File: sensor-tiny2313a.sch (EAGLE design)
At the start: 36 parts, among them IC1 TINY2313-*P*, M1 NRF24L01P-M, M2 DHT22, Q2 IRLML2502, U1 MCP1640C

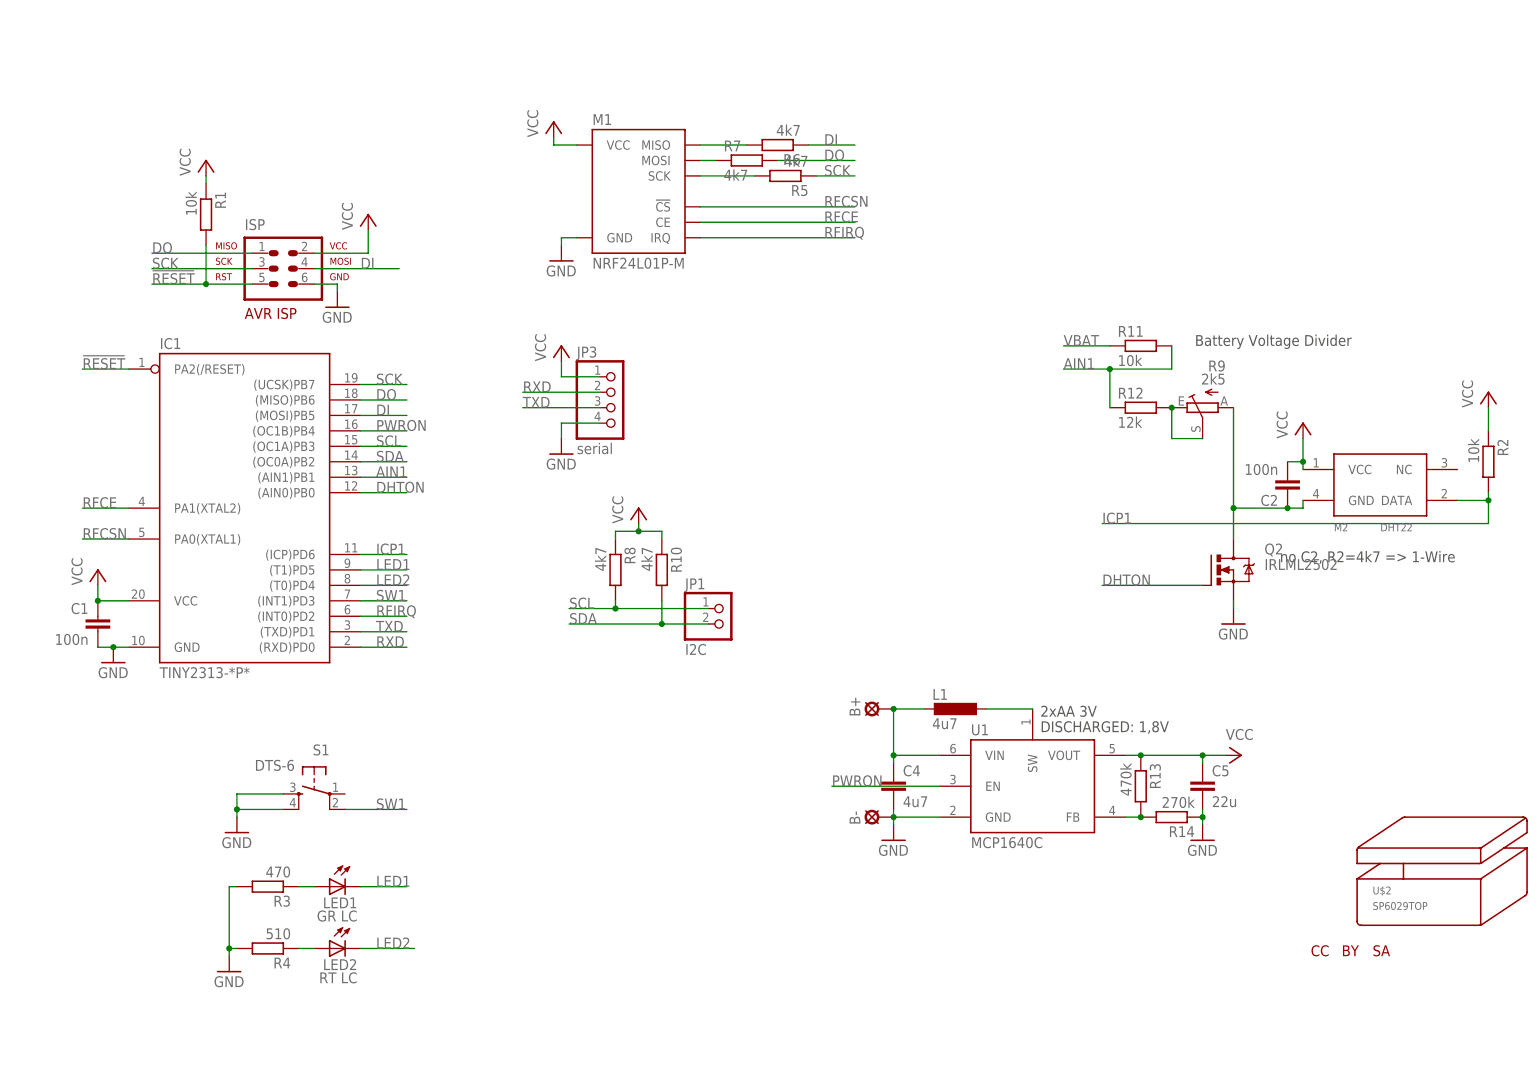
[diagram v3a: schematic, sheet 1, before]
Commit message: attiny so20 package
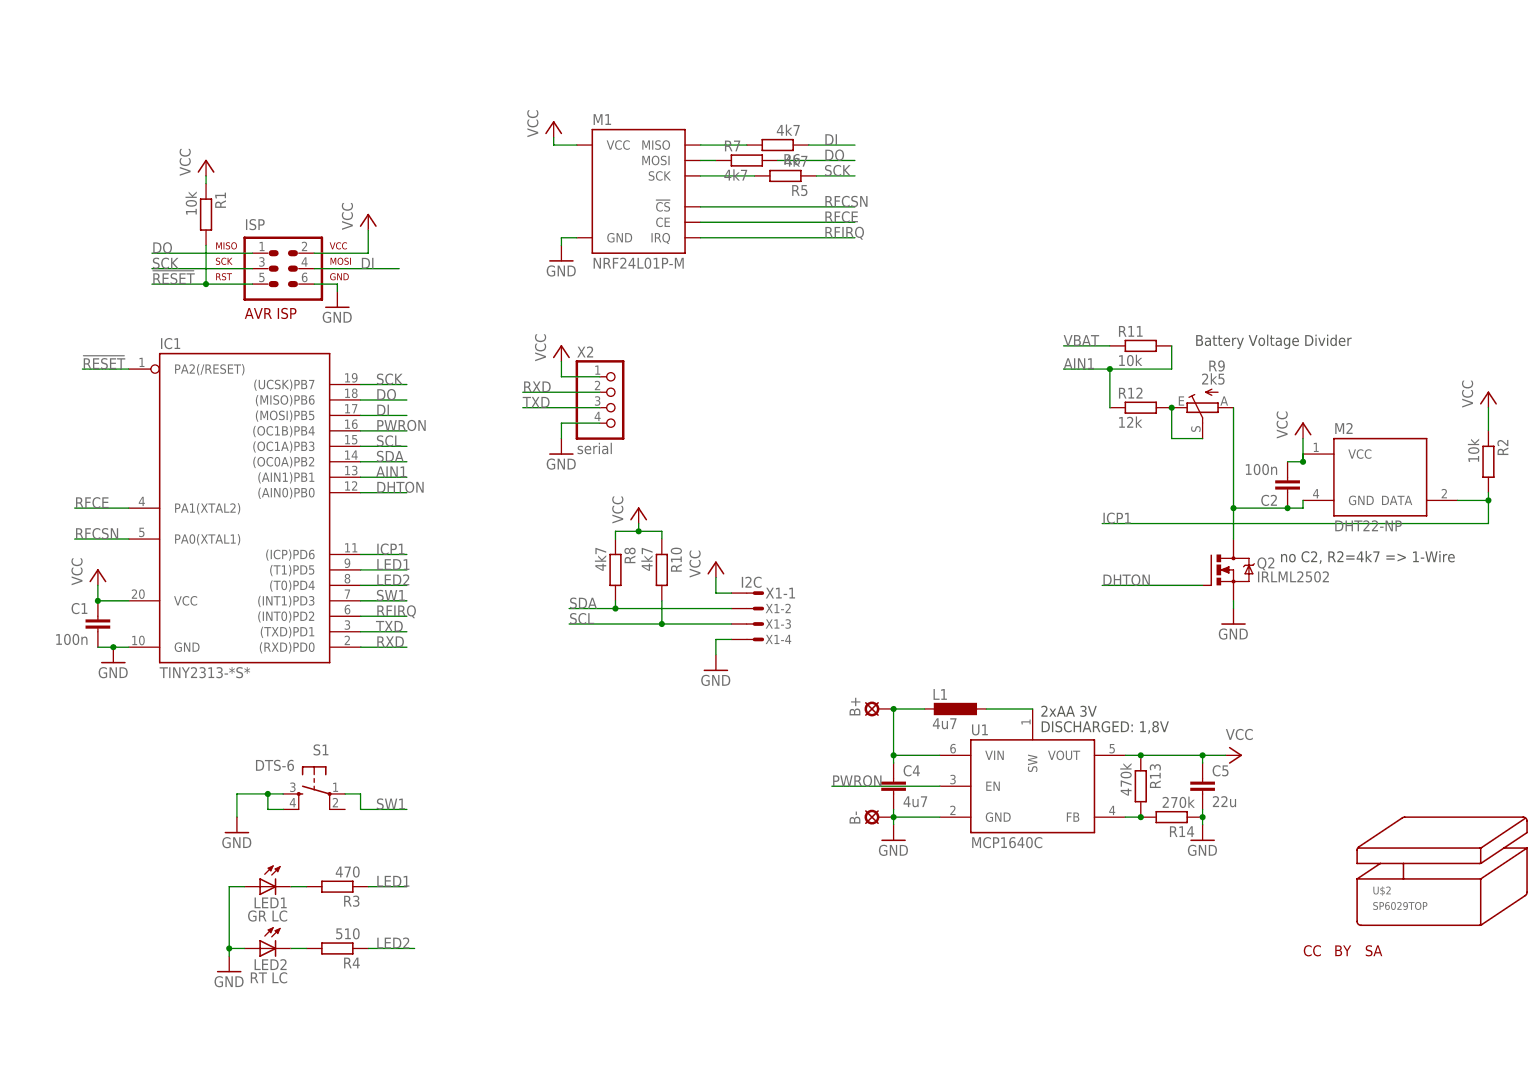
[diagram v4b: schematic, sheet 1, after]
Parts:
- removed JP1: I2C, pinhead-mod:PINHD-1X2_2.54
- added X1: I2C, con-amp-micromatch:MICROMATCH-4
- IC1: value TINY2313-*P* -> TINY2313-*S*; device avr-7:TINY2313-*P* -> avr-7:TINY2313-*S*
- M2: value DHT22 -> DHT22-NP; device modules:DHT22 -> modules:DHT22-NP
- R9: device pot:TRIM_EU-CA6V -> pot:TRIM_EU-CA6H
- U$1: value CC-TOP-HALF -> CC-TPLACE-HALF; device creative-commons:CC-TOP-HALF -> creative-commons:CC-TPLACE-HALF
- U$3: value BY-TOP-HALF -> BY-TPLACE-HS; device creative-commons:BY-TOP-HALF -> creative-commons:BY-TPLACE-HS
- U$4: value SA-TOP-HALF -> SA-TPLACE-HALF; device creative-commons:SA-TOP-HALF -> creative-commons:SA-TPLACE-HALF
- renumbered JP3 to X2
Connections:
- removed net N$13: LED1.A, R3.1
- new net N$3: LED1.C, R3.2
- net GND: now also LED1.A, LED2.A, X1-4.S; no longer R3.2, R4.2
- net LED1: now also R3.1; no longer LED1.C
- net LED2: now also R4.1; no longer LED2.C
- net N$1: now also LED2.C, R4.2; no longer LED2.A, R4.1
- net SCL: now also R10.2, X1-3.S; no longer JP1.1, R8.2
- net SDA: now also R8.2, X1-2.S; no longer JP1.2, R10.2
- net SW1: now also S1.1; no longer S1.2
- net VCC: now also X1-1.S
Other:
- moved on the sheet: LED1, LED2, R3, R4

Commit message: deleted second sch sheet with case scribbling
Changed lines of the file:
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@@
 <part name="R6" library="rcl" deviceset="R-EU_" device="R0603" value="4k7"/>
 <part name="R7" library="rcl" deviceset="R-EU_" device="R0603" value="4k7"/>
-<part name="FRAME1" library="frames" deviceset="A4L-LOC" device=""/>
 <part name="IC1" library="avr-7" deviceset="TINY2313*" device="-*S*" value="TINY2313-*S*"/>
 <part name="U$2" library="strapubox" deviceset="SP6029" device="TOP"/>
@@
 </nets>
 </sheet>
-<sheet>
-<plain>
-<wire x1="162.6" y1="55.6" x2="206.4" y2="55.6" width="0.4064" layer="97"/>
-<wire x1="206.4" y1="55.6" x2="206.4" y2="131.4" width="0.4064" layer="97"/>
-<wire x1="206.4" y1="131.4" x2="162.6" y2="131.4" width="0.4064" layer="97"/>
-<wire x1="162.6" y1="131.4" x2="162.6" y2="55.6" width="0.4064" layer="97"/>
-<circle x="172" y="64.5" radius="4" width="0.4064" layer="97"/>
-<circle x="197" y="64.5" radius="4" width="0.4064" layer="97"/>
-<circle x="172" y="122.5" radius="4" width="0.4064" layer="97"/>
-<circle x="197" y="122.5" radius="4" width="0.4064" layer="97"/>
-<rectangle x1="55" y1="38" x2="105" y2="52" layer="97" rot="R270"/>
-<rectangle x1="69" y1="38" x2="119" y2="52" layer="97" rot="R90"/>
-<rectangle x1="26" y1="8" x2="41" y2="33" layer="97" rot="R180"/>
-<rectangle x1="39.5" y1="57" x2="53.5" y2="90" layer="97" rot="R180"/>
-<wire x1="12.1" y1="7.1" x2="55.9" y2="7.1" width="0.4064" layer="97"/>
-<wire x1="55.9" y1="7.1" x2="55.9" y2="100.9" width="0.4064" layer="97"/>
-<wire x1="55.9" y1="100.9" x2="12.1" y2="100.9" width="0.4064" layer="97"/>
-<wire x1="12.1" y1="100.9" x2="12.1" y2="7.1" width="0.4064" layer="97"/>
-<circle x="50.5" y="12.5" radius="4.5" width="0.4064" layer="97"/>
-<circle x="17.5" y="95.5" radius="4.5" width="0.4064" layer="97"/>
-<circle x="17.5" y="12.5" radius="4.5" width="0.4064" layer="97"/>
-<circle x="50.5" y="95.5" radius="4.5" width="0.4064" layer="97"/>
-<circle x="20" y="21" radius="4" width="0.4064" layer="97"/>
-<circle x="48" y="21" radius="4" width="0.4064" layer="97"/>
-<circle x="20" y="87" radius="4" width="0.4064" layer="97"/>
-<circle x="48" y="87" radius="4" width="0.4064" layer="97"/>
-<rectangle x1="13" y1="33" x2="37.5" y2="87" layer="97"/>
-</plain>
-<instances>
-<instance part="FRAME1" gate="G$1" x="0" y="0"/>
-</instances>
-<busses>
-</busses>
-<nets>
-</nets>
-</sheet>
 </sheets>
-<errors>
-</errors>
 </schematic>
 </drawing>

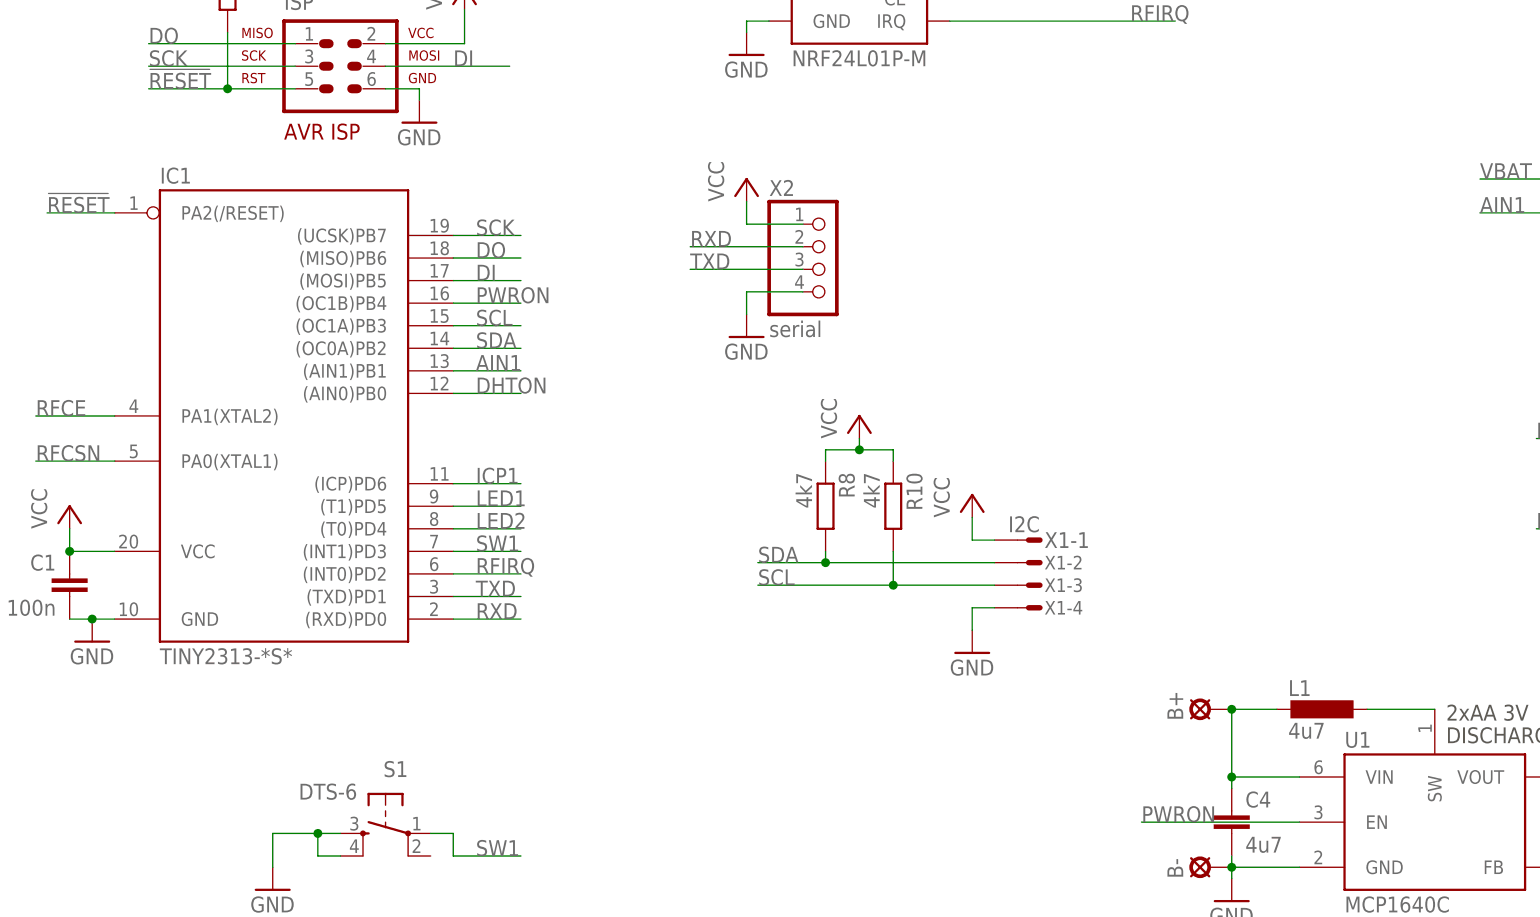
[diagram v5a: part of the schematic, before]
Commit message: renamed ic1->u1, u1->u2
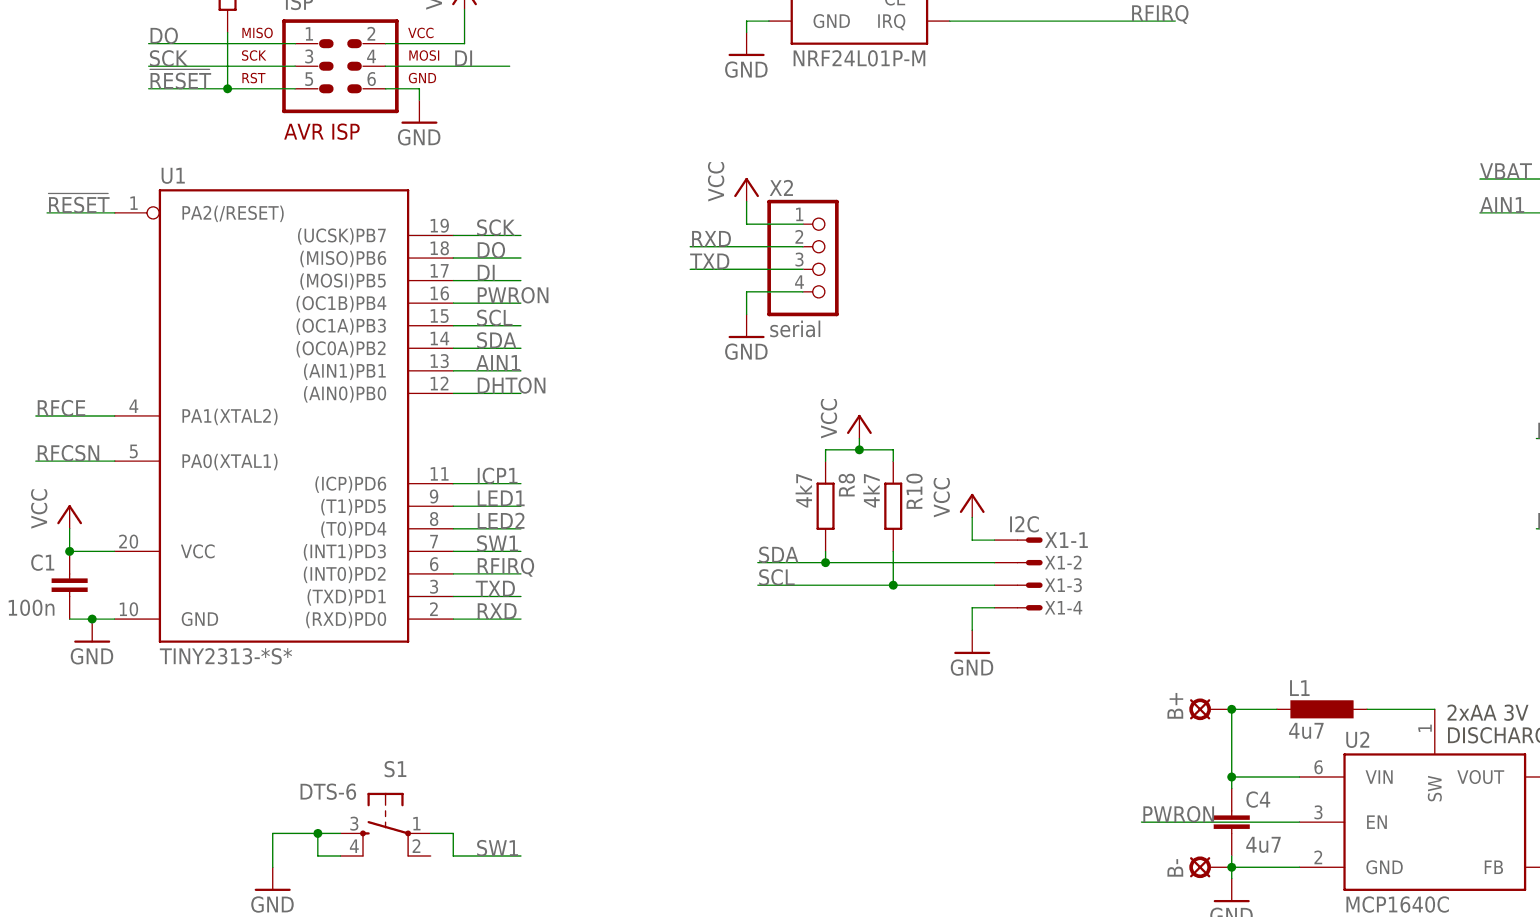
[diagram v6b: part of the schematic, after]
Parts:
- removed IC1: TINY2313-*S*, avr-7:TINY2313-*S*
- added U2: MCP1640C, karlnet-parts:MCP1640
- U1: value MCP1640C -> TINY2313-*S*; device karlnet-parts:MCP1640 -> avr-7:TINY2313-*S*
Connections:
- net !RESET: now also U1.PA2(/RESET); no longer IC1.PA2(/RESET)
- net AIN1: now also U1.(AIN1)PB1; no longer IC1.(AIN1)PB1
- net DHTON: now also U1.(AIN0)PB0; no longer IC1.(AIN0)PB0
- net DI: now also U1.(MOSI)PB5; no longer IC1.(MOSI)PB5
- net DO: now also U1.(MISO)PB6; no longer IC1.(MISO)PB6
- net GND: now also U2.GND; no longer IC1.GND
- net ICP1: now also U1.(ICP)PD6; no longer IC1.(ICP)PD6
- net LED1: now also U1.(T1)PD5; no longer IC1.(T1)PD5
- net LED2: now also U1.(T0)PD4; no longer IC1.(T0)PD4
- net N$8: now also U2.SW; no longer U1.SW
- net N$9: now also U2.FB; no longer U1.FB
- net PWRON: now also U1.(OC1B)PB4, U2.EN; no longer IC1.(OC1B)PB4, U1.EN
- net RFCE: now also U1.PA1(XTAL2); no longer IC1.PA1(XTAL2)
- net RFCSN: now also U1.PA0(XTAL1); no longer IC1.PA0(XTAL1)
- net RFIRQ: now also U1.(INT0)PD2; no longer IC1.(INT0)PD2
- net RXD: now also U1.(RXD)PD0; no longer IC1.(RXD)PD0
- net SCK: now also U1.(UCSK)PB7; no longer IC1.(UCSK)PB7
- net SCL: now also U1.(OC1A)PB3; no longer IC1.(OC1A)PB3
- net SDA: now also U1.(OC0A)PB2; no longer IC1.(OC0A)PB2
- net SW1: now also U1.(INT1)PD3; no longer IC1.(INT1)PD3
- net TXD: now also U1.(TXD)PD1; no longer IC1.(TXD)PD1
- net VBAT: now also U2.VIN; no longer U1.VIN
- net VCC: now also U1.VCC, U2.VOUT; no longer IC1.VCC, U1.VOUT

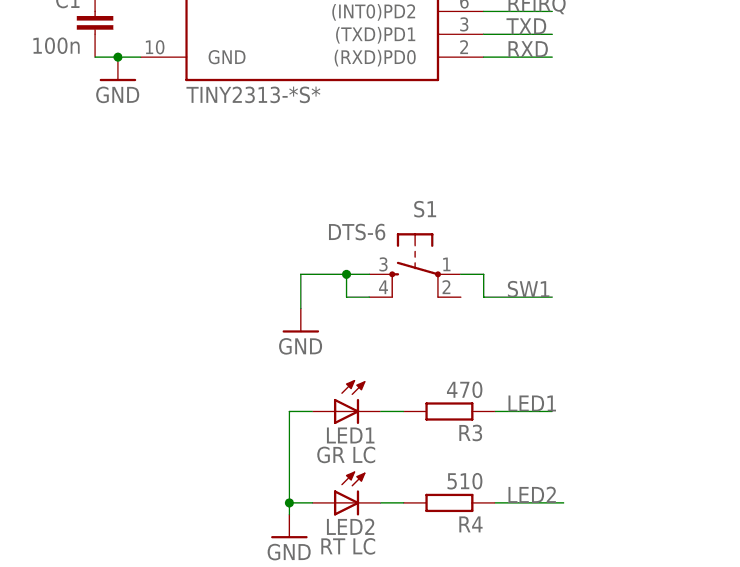
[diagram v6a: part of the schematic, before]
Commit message: gnd plane reshaped
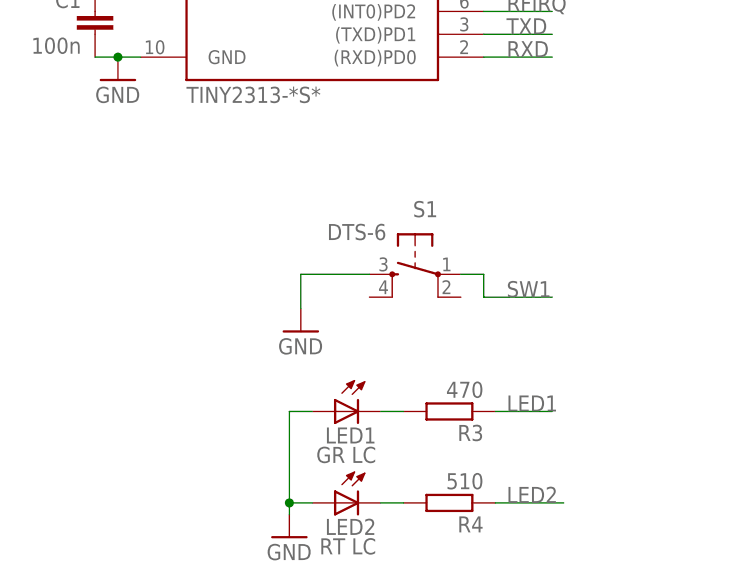
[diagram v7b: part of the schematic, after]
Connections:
- net GND: no longer S1.4
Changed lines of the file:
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@@
 <pinref part="GND8" gate="1" pin="GND"/>
 <pinref part="S1" gate="G$1" pin="3"/>
-<wire x1="49.53" y1="46.99" x2="46.99" y2="46.99" width="0.1524" layer="91"/>
-<wire x1="46.99" y1="46.99" x2="41.91" y2="46.99" width="0.1524" layer="91"/>
+<wire x1="49.53" y1="46.99" x2="41.91" y2="46.99" width="0.1524" layer="91"/>
 <wire x1="41.91" y1="46.99" x2="41.91" y2="43.18" width="0.1524" layer="91"/>
-<wire x1="46.99" y1="46.99" x2="46.99" y2="44.45" width="0.1524" layer="91"/>
-<junction x="46.99" y="46.99"/>
-<pinref part="S1" gate="G$1" pin="4"/>
-<wire x1="46.99" y1="44.45" x2="49.53" y2="44.45" width="0.1524" layer="91"/>
 </segment>
 <segment>
